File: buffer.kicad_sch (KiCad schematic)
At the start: 8 parts, among them J13 V_SIG, J14 Conn_01x02_Pin, J15 VSIG_BUF, U5 BUF634AIDR

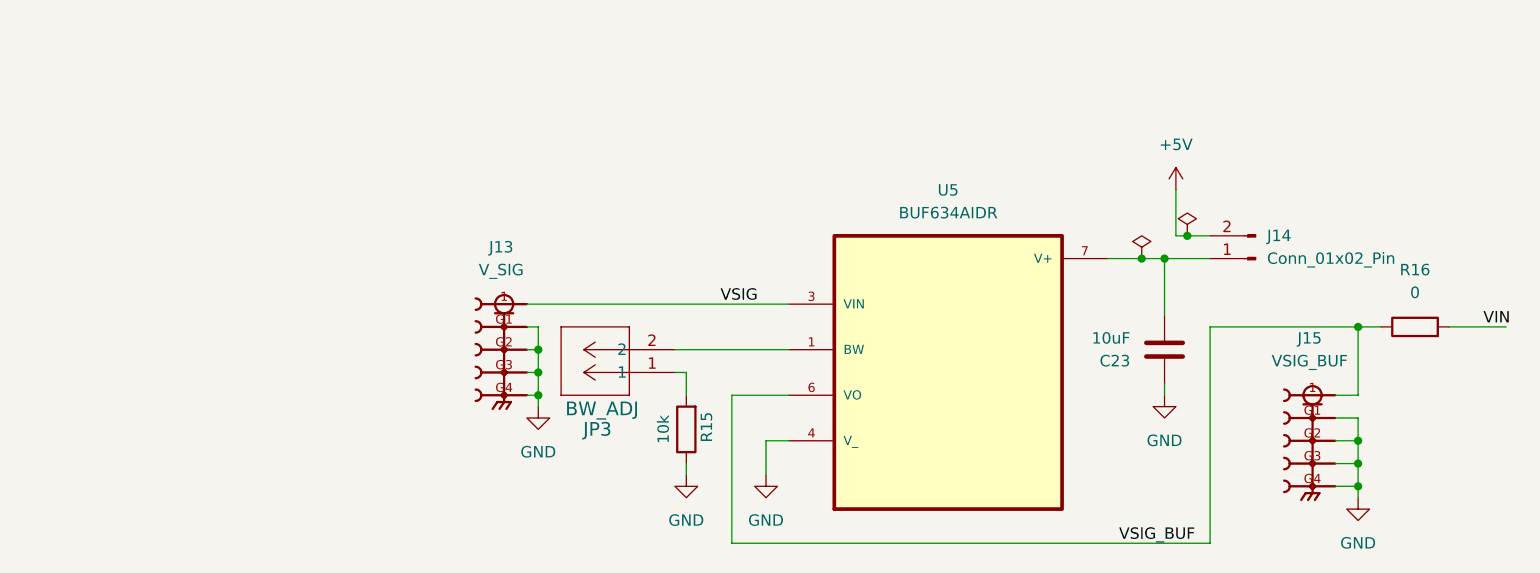
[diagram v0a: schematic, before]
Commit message: Add input filters to both current-sense amplifiers and rework the buffer power
- R29 to R32, in series with the INA190 inputs, change from 0 ohm to 100 ohm,
  and C24 and C25 (100n) go across each amplifier's IN+ and IN-. With the
  100 ohm resistors that is an 8 kHz differential filter on each.
- Buffer sheet. JP4 BUF_EN (2-pin header) replaces J14 between +5V and the
  BUF634A's V+. C23 becomes the 10u 1206 KEMET part, now from V+ to GND. The
  buffer's labels are global now, and R16 joins the buffer output to the VDD
  side of R4 (SHUNT_IN_A).
- One stub wire and its junction removed on the top sheet.

The netlist goes from 113 parts and 85 nets to 115 parts and 84 nets. ERC
shows 1 error, U5's V+ not driven behind JP4, left for the buffer rework along
with V- on GND and five parts that point at the demo board's libraries.
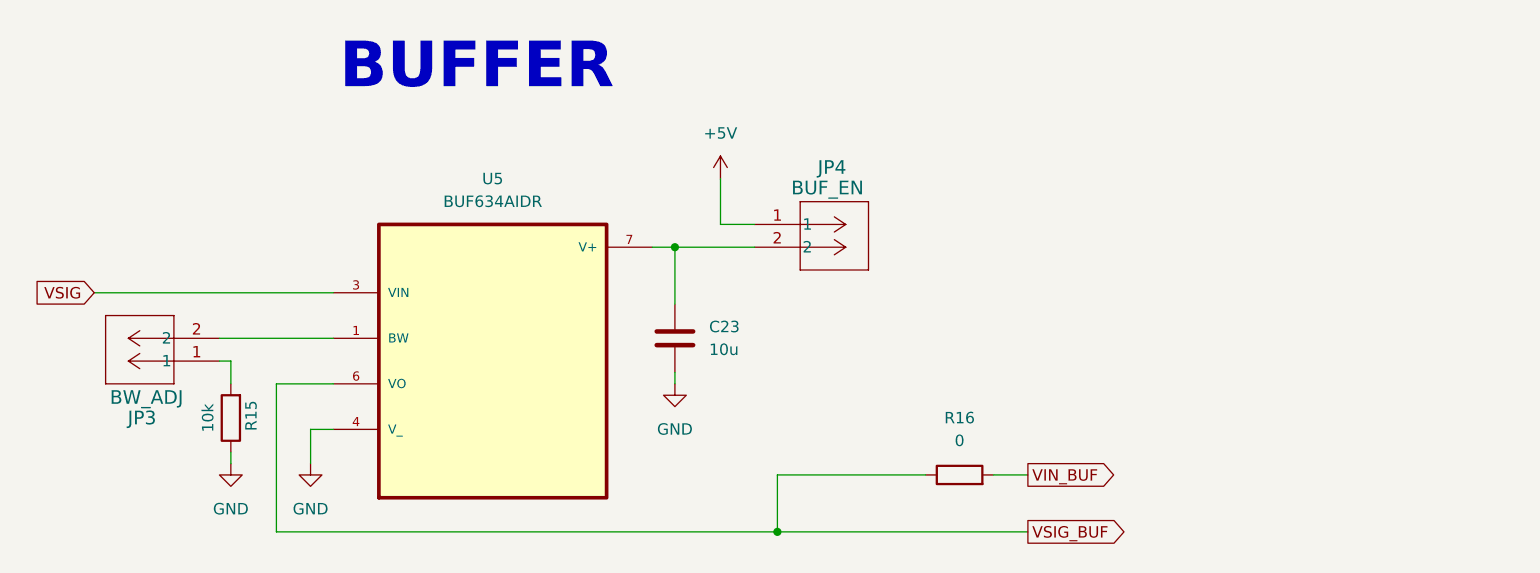
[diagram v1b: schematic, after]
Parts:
- removed J13: V_SIG, TPS7A7001_Evaluation_Board_footprint_lib:SAMTEC_SMA-J-P-H-ST-TH1, symbol SMA-J-P-H-ST-TH1:SMA-J-P-H-ST-TH1
- removed J14: Conn_01x02_Pin, Package_DIP:DIP-20_W7.62mm, symbol Connector:Conn_01x02_Pin
- removed J15: VSIG_BUF, SMA_J_P_H_ST_TH1:SAMTEC_SMA-J-P-H-ST-TH1, symbol SMA-J-P-H-ST-TH1:SMA-J-P-H-ST-TH1
- added JP4: BUF_EN, TPS7A7001_Evaluation_Board_footprint_lib:CONN_PxC02S_SUL, symbol PEC02SAAN:PEC02SAAN
- C23: value 10uF -> 10u; footprint Capacitor_SMD:C_0805_2012Metric_Pad1.18x1.45mm_HandSolder -> Capacitor_SMD:C_1206_3216Metric_Pad1.33x1.80mm_HandSolder; Distributer Link 1 https://www.digikey.com/en/products/detail/kemet/C0805C106K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 -> https://www.digikey.com/en/products/detail/kemet/C1206C106J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; Distributer Link 2 https://www.mouser.com/en/ProductDetail/KEMET/C0805C106K8RA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 -> (none); Manufacturer Part Number C0805C106K8RACTU -> C1206C106J3RACAUTO
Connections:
- net +5V: now also JP4.1
- net GND: now also C23.2; no longer C23.1
- net at U5.7 (V+): now also C23.1, JP4.2; no longer C23.2
- net VIN renamed VIN_BUF
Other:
- note added: "BUFFER"
- moved on the sheet: JP3, R15, R16, U5
